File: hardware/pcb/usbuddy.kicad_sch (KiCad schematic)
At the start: 11 parts, among them J1 USB_A, SW1 SW_Push, U1 CH552G, U2 ER_OLEDM0.91_1x-I2C

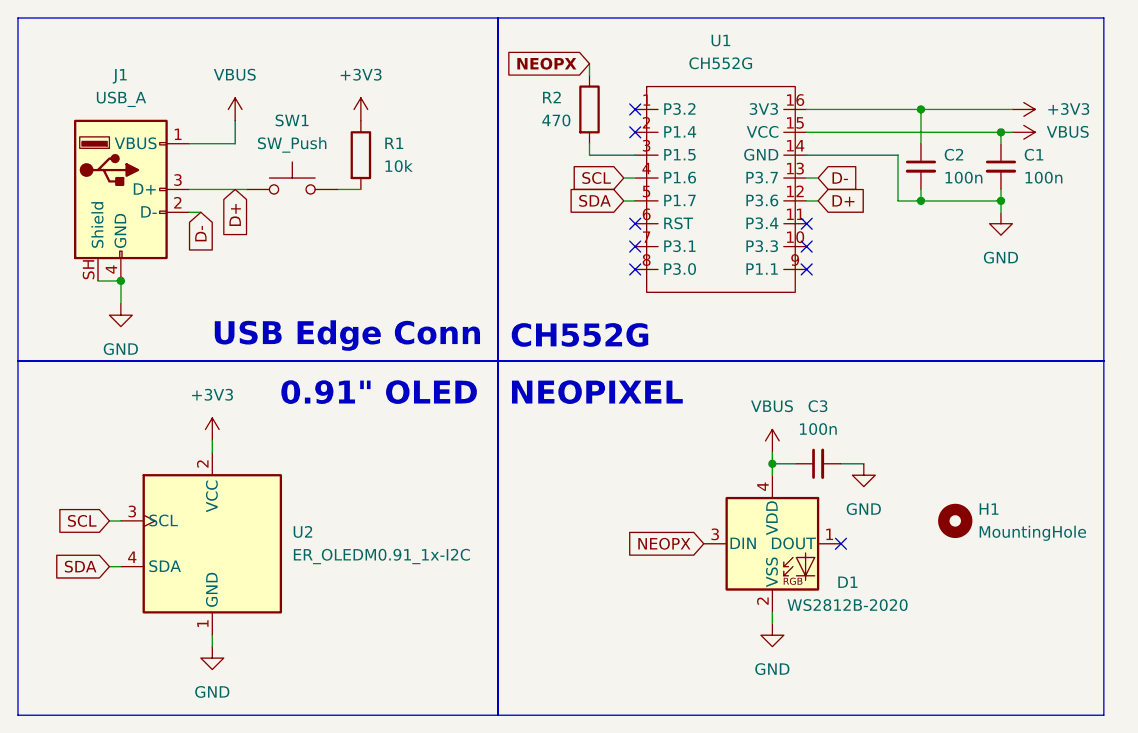
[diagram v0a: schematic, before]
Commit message: update design to use green static LED
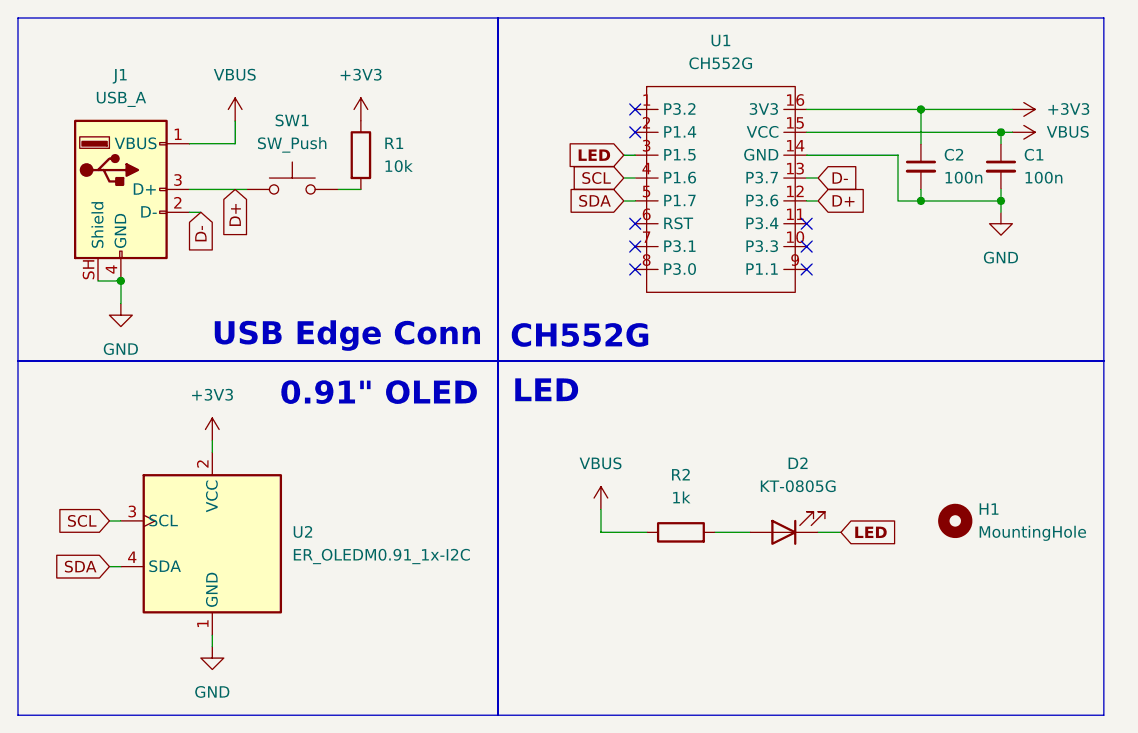
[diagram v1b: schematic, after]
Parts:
- removed C3: 100n, Capacitor_SMD:C_0603_1608Metric, symbol Device:C_Small
- removed D1: WS2812B-2020, LED_SMD:LED_WS2812B-2020_PLCC4_2.0x2.0mm, symbol LED:WS2812B-2020
- added D2: KT-0805G, LED_SMD:LED_0805_2012Metric, symbol Device:LED
- R2: value 470 -> 1k
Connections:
- net NEOPX is gone; now on net VBUS: R2.1
- net at R2.2: now also D2.2 (A); no longer U1.3 (P1.5)
- new net LED: D2.1 (K), U1.3 (P1.5)
- no-connect marks 9 -> 8
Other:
- note added: "LED"
- note removed: "NEOPIXEL"
